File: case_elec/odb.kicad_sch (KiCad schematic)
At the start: 5 parts

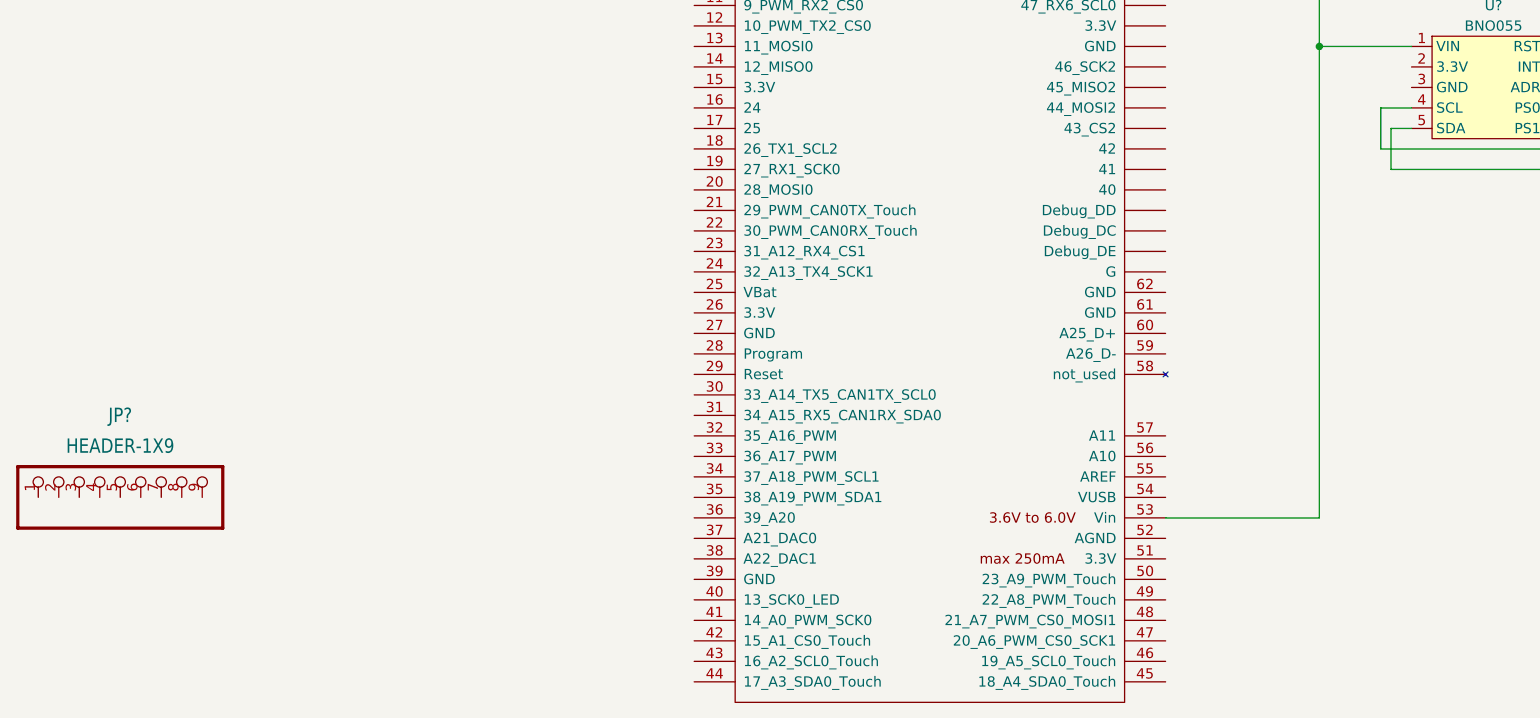
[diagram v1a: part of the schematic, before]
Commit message: Connexion SDA/SCL
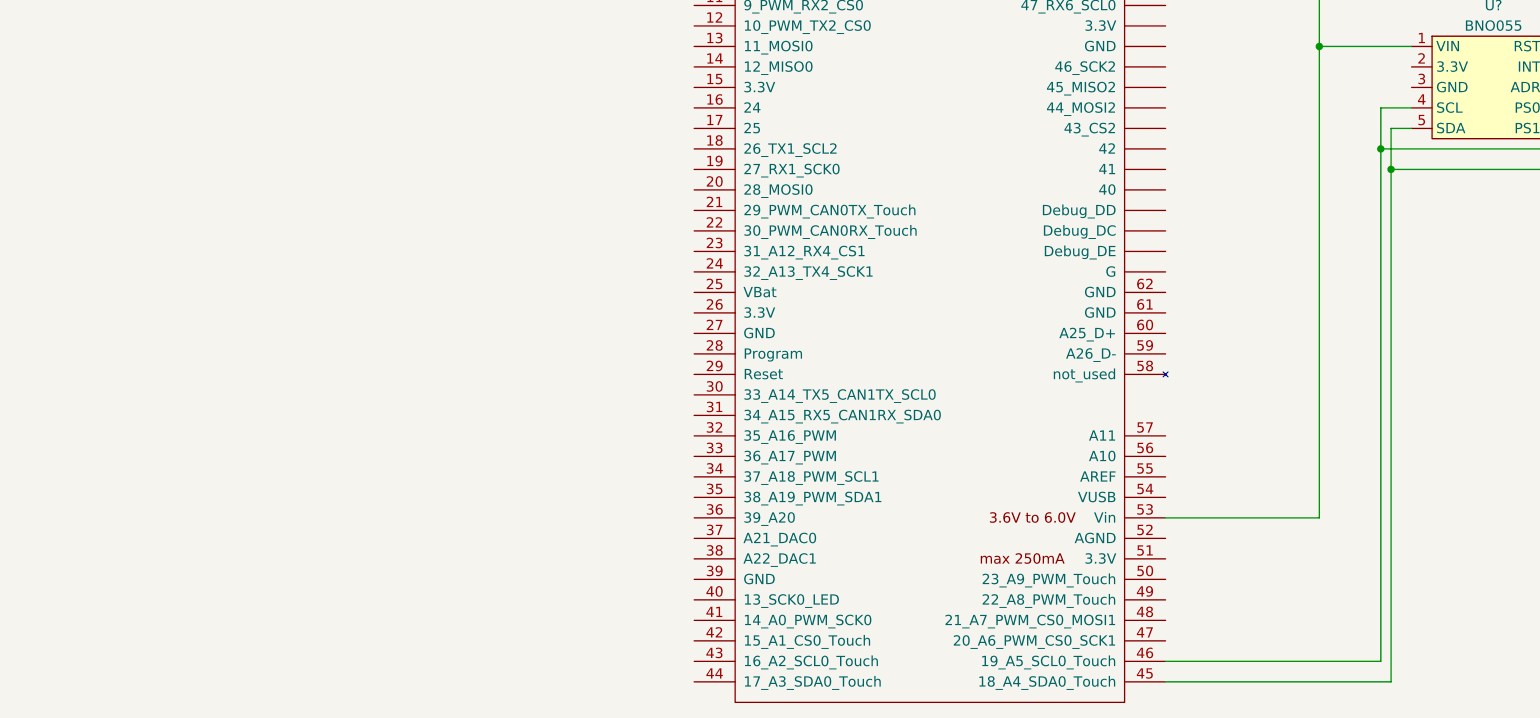
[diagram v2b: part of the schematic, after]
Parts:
- removed JP?: HEADER-1X9, PCB_case_elec:1X09_OVAL, symbol PCB_case_elec-eagle-import:HEADER-1X9
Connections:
- net at U?.5 (SDA), U?.7 (SDA): now also U?.45 (18_A4_SDA0_Touch)
- net at U?.4 (SCL), U?.8 (SCL): now also U?.46 (19_A5_SCL0_Touch)
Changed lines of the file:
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@@
   (junction (at 226.06 40.64) (diameter 0) (color 0 0 0 0)
   )
+  (junction (at 198.12 101.6) (diameter 0) (color 0 0 0 0)
+  )
   (junction (at 189.23 62.23) (diameter 0) (color 0 0 0 0)
   )
   (junction (at 189.23 86.36) (diameter 0) (color 0 0 0 0)
   )
+  (junction (at 196.85 99.06) (diameter 0) (color 0 0 0 0)
+  )
   (wire (pts (xy 222.25 101.6) (xy 198.12 101.6))
     (stroke (width 0) (type default) (color 0 0 0 0))
@@
     (stroke (width 0) (type default) (color 0 0 0 0))
   )
+  (wire (pts (xy 170.18 165.1) (xy 198.12 165.1))
+    (stroke (width 0) (type default) (color 0 0 0 0))
+  )
   (wire (pts (xy 92.71 60.96) (xy 92.71 26.67))
     (stroke (width 0) (type default) (color 0 0 0 0))
@@
     (stroke (width 0) (type default) (color 0 0 0 0))
   )
+  (wire (pts (xy 198.12 165.1) (xy 198.12 101.6))
+    (stroke (width 0) (type default) (color 0 0 0 0))
+  )
   (wire (pts (xy 220.98 27.94) (xy 220.98 35.56))
     (stroke (width 0) (type default) (color 0 0 0 0))
@@
     (stroke (width 0) (type default) (color 0 0 0 0))
   )
+  (wire (pts (xy 196.85 162.56) (xy 196.85 99.06))
+    (stroke (width 0) (type default) (color 0 0 0 0))
+  )
   (wire (pts (xy 219.71 40.64) (xy 226.06 40.64))
     (stroke (width 0) (type default) (color 0 0 0 0))
   )
   (wire (pts (xy 111.76 60.96) (xy 92.71 60.96))
+    (stroke (width 0) (type default) (color 0 0 0 0))
+  )
+  (wire (pts (xy 170.18 162.56) (xy 196.85 162.56))
     (stroke (width 0) (type default) (color 0 0 0 0))
   )
@@
     (pin "~")
   )
-  (symbol (lib_id "PCB_case_elec-eagle-import:HEADER-1X9") (at 40.64 139.7 90) (unit 1)
-    (in_bom yes) (on_board yes) (fields_autoplaced)
-    (property "Reference" "JP?" (id 0) (at 40.64 132.08 90)
-      (effects (font (size 1.778 1.5113)))
-    )
-    (property "Value" "HEADER-1X9" (id 1) (at 40.64 135.89 90)
-      (effects (font (size 1.778 1.5113)))
-    )
-    (property "Footprint" "PCB_case_elec:1X09_OVAL" (id 2) (at 40.64 139.7 0)
-      (effects (font (size 1.27 1.27)) hide)
-    )
-    (property "Datasheet" "" (id 3) (at 40.64 139.7 0)
+  (symbol (lib_id "Adafruit_sensors:Ultimate_GPS") (at 210.82 41.91 0) (unit 1)
+    (in_bom yes) (on_board yes)
+    (property "Reference" "U?" (id 0) (at 210.82 30.48 0))
+    (property "Value" "Ultimate_GPS" (id 1) (at 212.09 33.02 0))
+    (property "Footprint" "" (id 2) (at 203.835 34.29 0)
+      (effects (font (size 1.27 1.27)) hide)
+    )
+    (property "Datasheet" "" (id 3) (at 203.835 34.29 0)
       (effects (font (size 1.27 1.27)) hide)
     )
     (pin "1")
+    (pin "2")
+    (pin "3")
+    (pin "4")
+    (pin "4")
+    (pin "5")
+    (pin "6")
+    (pin "7")
+    (pin "8")
+  )
+  (symbol (lib_name "BNO055_1") (lib_id "Adafruit_sensors:BNO055") (at 210.82 91.44 0) (unit 1)
+    (in_bom yes) (on_board yes)
+    (property "Reference" "U?" (id 0) (at 210.82 81.28 0))
+    (property "Value" "BNO055" (id 1) (at 210.82 83.82 0))
+    (property "Footprint" "" (id 2) (at 203.2 86.36 0)
+      (effects (font (size 1.27 1.27)) hide)
+    )
+    (property "Datasheet" "" (id 3) (at 203.2 86.36 0)
+      (effects (font (size 1.27 1.27)) hide)
+    )
+    (pin "1")
+    (pin "10")
     (pin "2")
     (pin "3")
@@
     (pin "9")
   )
-  (symbol (lib_id "Adafruit_sensors:Ultimate_GPS") (at 210.82 41.91 0) (unit 1)
-    (in_bom yes) (on_board yes)
-    (property "Reference" "U?" (id 0) (at 210.82 30.48 0))
-    (property "Value" "Ultimate_GPS" (id 1) (at 212.09 33.02 0))
-    (property "Footprint" "" (id 2) (at 203.835 34.29 0)
-      (effects (font (size 1.27 1.27)) hide)
-    )
-    (property "Datasheet" "" (id 3) (at 203.835 34.29 0)
-      (effects (font (size 1.27 1.27)) hide)
-    )
-    (pin "1")
-    (pin "2")
-    (pin "3")
-    (pin "4")
-    (pin "4")
-    (pin "5")
-    (pin "6")
-    (pin "7")
-    (pin "8")
-  )
-  (symbol (lib_name "BNO055_1") (lib_id "Adafruit_sensors:BNO055") (at 210.82 91.44 0) (unit 1)
-    (in_bom yes) (on_board yes)
-    (property "Reference" "U?" (id 0) (at 210.82 81.28 0))
-    (property "Value" "BNO055" (id 1) (at 210.82 83.82 0))
-    (property "Footprint" "" (id 2) (at 203.2 86.36 0)
-      (effects (font (size 1.27 1.27)) hide)
-    )
-    (property "Datasheet" "" (id 3) (at 203.2 86.36 0)
-      (effects (font (size 1.27 1.27)) hide)
-    )
-    (pin "1")
-    (pin "10")
-    (pin "2")
-    (pin "3")
-    (pin "4")
-    (pin "5")
-    (pin "6")
-    (pin "7")
-    (pin "8")
-    (pin "9")
-  )
   (sheet_instances
     (path "/" (page "1"))
   )
   (symbol_instances
-    (path "/74241264-0098-4d88-8365-65d717f7e09d"
-      (reference "JP?") (unit 1) (value "HEADER-1X9") (footprint "PCB_case_elec:1X09_OVAL")
-    )
     (path "/4324021c-adf2-48f1-8a00-7ea1c3478302"
       (reference "U?") (unit 1) (value "MPL3115A") (footprint "")
